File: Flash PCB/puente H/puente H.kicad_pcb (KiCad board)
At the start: 2 copper layers, 19 x 18 mm, 7 parts, among them IC1 TB6612FNG, J1 HEADER_8, J3 HEADER_8

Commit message: Arreglando errores de diseño
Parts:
- C3: footprint Capacitor_Tantalum_SMD:CP_EIA-2012-12_Kemet-R_Pad1.30x1.05mm_HandSolder -> Capacitor_Tantalum_SMD:CP_EIA-3528-21_Kemet-B_Pad1.50x2.35mm_HandSolder
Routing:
- net Earth: track 3.96 -> 7.92 mm
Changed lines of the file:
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@@
     (pad_to_mask_clearance 0)
     (pcbplotparams
-      (layerselection 0x00010fc_ffffffff)
+      (layerselection 0x0000000_7fffffff)
       (plot_on_all_layers_selection 0x0000000_00000000)
       (disableapertmacros false)
@@
       (sketchpadsonfab false)
       (subtractmaskfromsilk false)
-      (outputformat 1)
-      (mirror false)
-      (drillshape 1)
+      (outputformat 5)
+      (mirror true)
+      (drillshape 0)
       (scaleselection 1)
       (outputdirectory "")
@@
   (net 13 "/AIN2")
   (net 14 "/PWMA")
-  (footprint "Capacitor_Tantalum_SMD:CP_EIA-2012-12_Kemet-R_Pad1.30x1.05mm_HandSolder" (layer "F.Cu")
+  (footprint "Capacitor_Tantalum_SMD:CP_EIA-3528-21_Kemet-B_Pad1.50x2.35mm_HandSolder" (layer "F.Cu")
     (at 144.231 90.424)
-    (descr "Tantalum Capacitor SMD Kemet-R (2012-12 Metric), IPC_7351 nominal, (Body size from: https://www.vishay.com/docs/40182/tmch.pdf), generated with kicad-footprint-generator")
+    (descr "Tantalum Capacitor SMD Kemet-B (3528-21 Metric), IPC_7351 nominal, (Body size from: http://www.kemet.com/Lists/ProductCatalog/Attachments/253/KEM_TC101_STD.pdf), generated with kicad-footprint-generator")
     (tags "capacitor tantalum")
     (property "Sheetfile" "puente H.kicad_sch")
@@
     (property "ki_keywords" "cap capacitor")
     (attr smd)
-    (fp_text reference "C3" (at 0 -1.58) (layer "F.SilkS")
+    (fp_text reference "C3" (at 0 -2.35) (layer "F.SilkS")
         (effects (font (size 1 1) (thickness 0.15)))
     )
-    (fp_text value "10uF" (at 0 1.58) (layer "F.Fab")
+    (fp_text value "10uF" (at 0 2.35) (layer "F.Fab")
         (effects (font (size 1 1) (thickness 0.15)))
     )
     (fp_text user "${REFERENCE}" (at 0 0) (layer "F.Fab")
-        (effects (font (size 0.5 0.5) (thickness 0.08)))
+        (effects (font (size 0.88 0.88) (thickness 0.13)))
     )
-    (fp_line (start -1.885 -0.785) (end -1.885 0.785)
+    (fp_line (start -2.635 -1.51) (end -2.635 1.51)
       (stroke (width 0.12) (type solid)) (layer "F.SilkS"))
-    (fp_line (start -1.885 0.785) (end 1 0.785)
+    (fp_line (start -2.635 1.51) (end 1.75 1.51)
       (stroke (width 0.12) (type solid)) (layer "F.SilkS"))
-    (fp_line (start 1 -0.785) (end -1.885 -0.785)
+    (fp_line (start 1.75 -1.51) (end -2.635 -1.51)
       (stroke (width 0.12) (type solid)) (layer "F.SilkS"))
-    (fp_line (start -1.88 -0.88) (end 1.88 -0.88)
+    (fp_line (start -2.62 -1.65) (end 2.62 -1.65)
       (stroke (width 0.05) (type solid)) (layer "F.CrtYd"))
-    (fp_line (start -1.88 0.88) (end -1.88 -0.88)
+    (fp_line (start -2.62 1.65) (end -2.62 -1.65)
       (stroke (width 0.05) (type solid)) (layer "F.CrtYd"))
-    (fp_line (start 1.88 -0.88) (end 1.88 0.88)
+    (fp_line (start 2.62 -1.65) (end 2.62 1.65)
       (stroke (width 0.05) (type solid)) (layer "F.CrtYd"))
-    (fp_line (start 1.88 0.88) (end -1.88 0.88)
+    (fp_line (start 2.62 1.65) (end -2.62 1.65)
       (stroke (width 0.05) (type solid)) (layer "F.CrtYd"))
-    (fp_line (start -1 -0.3125) (end -1 0.625)
+    (fp_line (start -1.75 -0.7) (end -1.75 1.4)
       (stroke (width 0.1) (type solid)) (layer "F.Fab"))
-    (fp_line (start -1 0.625) (end 1 0.625)
+    (fp_line (start -1.75 1.4) (end 1.75 1.4)
       (stroke (width 0.1) (type solid)) (layer "F.Fab"))
-    (fp_line (start -0.6875 -0.625) (end -1 -0.3125)
+    (fp_line (start -1.05 -1.4) (end -1.75 -0.7)
       (stroke (width 0.1) (type solid)) (layer "F.Fab"))
-    (fp_line (start 1 -0.625) (end -0.6875 -0.625)
+    (fp_line (start 1.75 -1.4) (end -1.05 -1.4)
       (stroke (width 0.1) (type solid)) (layer "F.Fab"))
-    (fp_line (start 1 0.625) (end 1 -0.625)
+    (fp_line (start 1.75 1.4) (end 1.75 -1.4)
       (stroke (width 0.1) (type solid)) (layer "F.Fab"))
-    (pad "1" smd roundrect (at -0.975 0) (size 1.3 1.05) (layers "F.Cu" "F.Paste" "F.Mask") (roundrect_rratio 0.238095)
+    (pad "1" smd roundrect (at -1.625 0) (size 1.5 2.35) (layers "F.Cu" "F.Paste" "F.Mask") (roundrect_rratio 0.1666673333)
       (net 3 "/VM1") (pintype "passive"))
-    (pad "2" smd roundrect (at 0.975 0) (size 1.3 1.05) (layers "F.Cu" "F.Paste" "F.Mask") (roundrect_rratio 0.238095)
+    (pad "2" smd roundrect (at 1.625 0) (size 1.5 2.35) (layers "F.Cu" "F.Paste" "F.Mask") (roundrect_rratio 0.1666673333)
       (net 1 "Earth") (pintype "passive"))
-    (model "${KICAD6_3DMODEL_DIR}/Capacitor_Tantalum_SMD.3dshapes/CP_EIA-2012-12_Kemet-R.wrl"
+    (model "${KICAD6_3DMODEL_DIR}/Capacitor_Tantalum_SMD.3dshapes/CP_EIA-3528-21_Kemet-B.wrl"
       (offset (xyz 0 0 0))
       (scale (xyz 1 1 1))
@@
     (style (thickness 0.15) (arrow_length 1.27) (text_position_mode 0) (extension_height 0.58642) (extension_offset 0.5) keep_text_aligned)
   )
-  (segment (start 140.3858 101.8794) (end 142.367 101.8794) (width 1) (layer "F.Cu") (net 1))
-  (segment (start 140.2588 98.044) (end 142.24 98.044) (width 1) (layer "F.Cu") (net 1))
+  (segment (start 146.1262 92.964) (end 147.2438 92.964) (width 1) (layer "F.Cu") (net 1))
+  (segment (start 141.1986 92.075) (end 141.9098 92.075) (width 1) (layer "F.Cu") (net 1))
+  (segment (start 142.3416 92.5068) (end 142.3416 93.0148) (width 1) (layer "F.Cu") (net 1))
+  (segment (start 141.9098 92.075) (end 142.3416 92.5068) (width 1) (layer "F.Cu") (net 1))
+  (segment (start 140.6144 101.9302) (end 142.5956 101.9302) (width 1) (layer "F.Cu") (net 1))
+  (segment (start 147.2438 92.964) (end 147.955 92.2528) (width 1) (layer "F.Cu") (net 1))
+  (segment (start 140.5128 98.0186) (end 142.494 98.0186) (width 1) (layer "F.Cu") (net 1))
   (segment (start 137.16 92.3676) (end 139.4846 92.3676) (width 0.25) (layer "F.Cu") (net 2))
   (segment (start 142.3416 95.6056) (end 145.7354 98.9994) (width 0.25) (layer "F.Cu") (net 2))

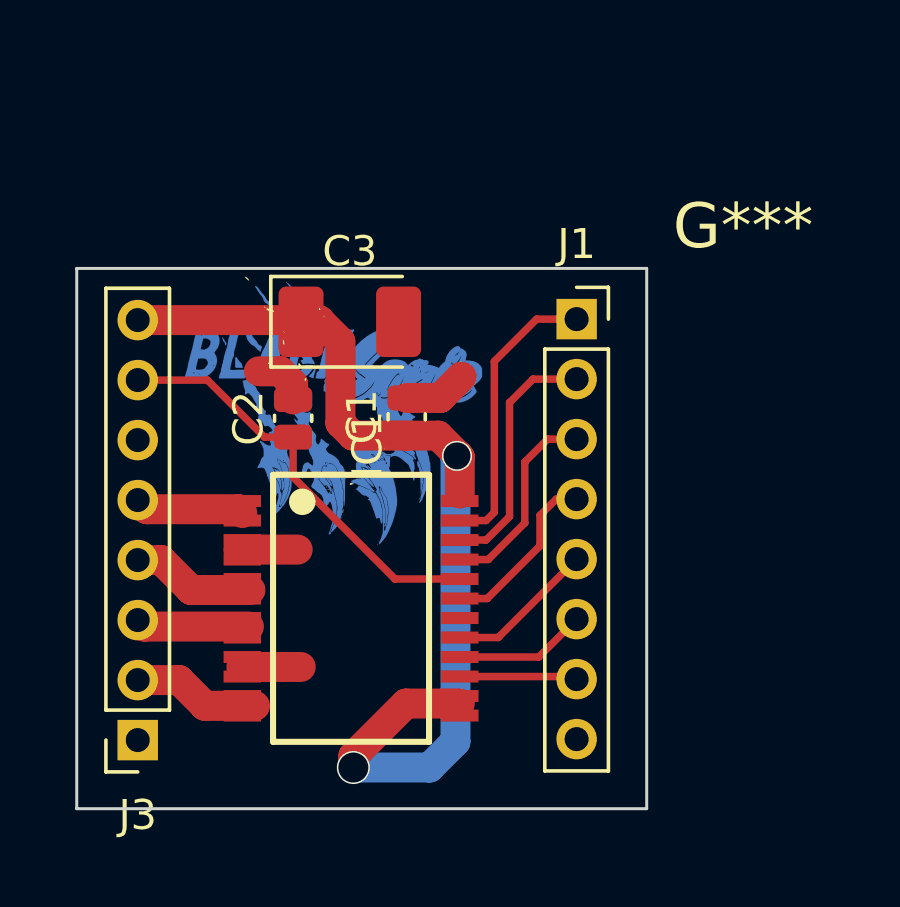
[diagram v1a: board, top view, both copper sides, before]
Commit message: Arreglando Puente H
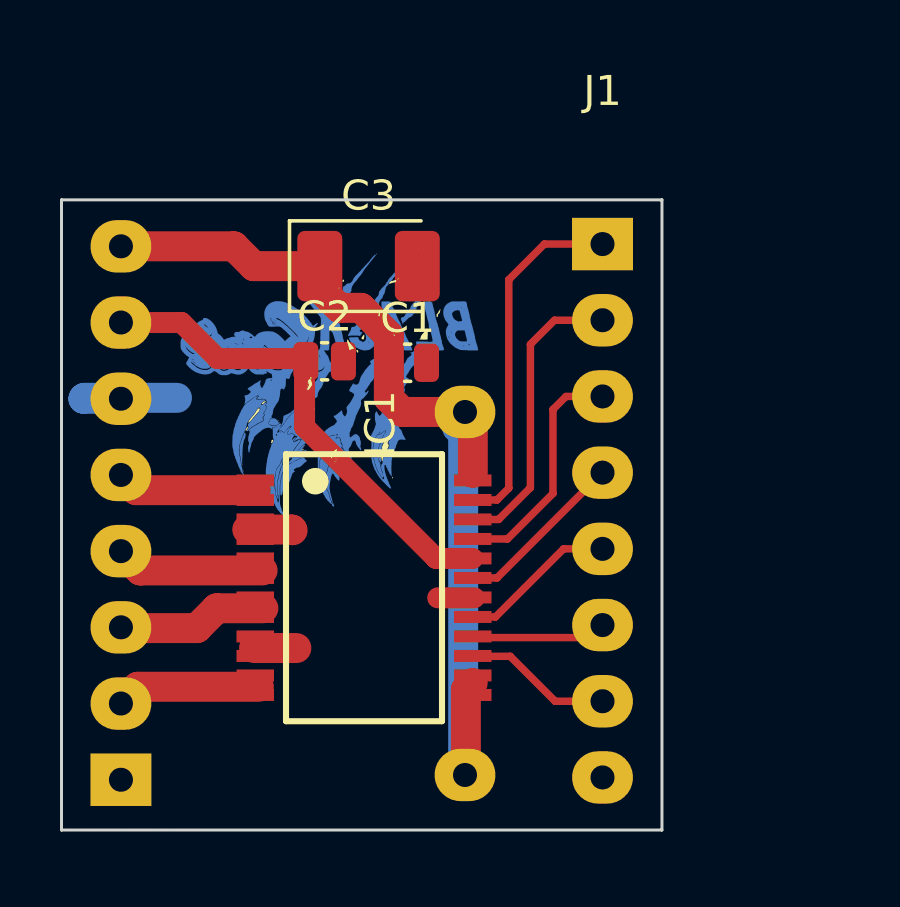
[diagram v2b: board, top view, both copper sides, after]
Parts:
- added ?: , , F.Cu at (148.1, 105.5)
- added ?: , , F.Cu at (148.1, 93.4)
- J1, J3: footprint Connector_PinSocket_2.00mm:PinSocket_1x08_P2.00mm_Vertical -> EESTN5:Pin_Header_Angled_1x08
- moved J3 7.59 mm to (136.6, 96.8)
- moved J1 6.45 mm to (152.7, 96.7)
- moved C2 2.17 mm to (143.4, 91.7), turned to 0 degrees
- moved C3 1.96 mm to (144.9, 88.6)
- moved C1 1.80 mm to (146.2, 91.8), turned to 0 degrees
- moved G*** 1.04 mm to (143.4, 92.3)
- moved IC1 0.81 mm to (144.7, 99.3)
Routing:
- net /PWMA: track 9.62 -> 11.9 mm
- net VCC: track 14.3 -> 16.2 mm
- net /AIN2: track 8.34 -> 9.88 mm
- net /B02: track 3.80 -> 5.03 mm
- net /AIN1: track 6.75 -> 7.93 mm
- net /A01: track 3.67 -> 4.71 mm
- net /PWMB: track 3.93 -> 4.95 mm
- net /A02: track 4.17 -> 4.99 mm
- net Earth: track 7.92 -> 8.54 mm
- net /B01: track 4.27 -> 4.83 mm
- net /VM1: track 33.4 -> 33.1 mm, vias 2 -> 0
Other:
- board size 19 x 18 mm -> 20 x 21 mm
